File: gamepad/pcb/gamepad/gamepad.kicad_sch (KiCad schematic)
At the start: 9 parts, among them U1 Pico

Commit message: upt(gamepad): working on pcb
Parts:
- renumbered ButtonConnector1 to dPad_east1, ButtonConnector6 to dPad_north1, ButtonConnector2 to dPad_south1, ButtonConnector3 to dPad_west1, JoystickConnector2 to joystick_left1, JoystickConnector1 to joystick_right1, ButtonConnector5 to operators_minus1, ButtonConnector4 to operators_plus1
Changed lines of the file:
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@@
 		(dnp no)
 		(fields_autoplaced yes)
-		(property "Reference" "ButtonConnector4"
+		(property "Reference" "operators_plus1"
 			(at 158.75 111.7599 0)
 			(effects
@@
 			(project "gamepad"
 				(path "/00bcd25f-2f85-4197-8989-5ad786ea0927"
-					(reference "ButtonConnector4")
+					(reference "operators_plus1")
 					(unit 1)
 				)
@@
 		(dnp no)
 		(fields_autoplaced yes)
-		(property "Reference" "ButtonConnector1"
+		(property "Reference" "dPad_east1"
 			(at 158.75 92.7099 0)
 			(effects
@@
 			(project "gamepad"
 				(path "/00bcd25f-2f85-4197-8989-5ad786ea0927"
-					(reference "ButtonConnector1")
+					(reference "dPad_east1")
 					(unit 1)
 				)
@@
 		(dnp no)
 		(fields_autoplaced yes)
-		(property "Reference" "JoystickConnector2"
+		(property "Reference" "joystick_left1"
 			(at 158.75 128.2699 0)
 			(effects
@@
 			(project ""
 				(path "/00bcd25f-2f85-4197-8989-5ad786ea0927"
-					(reference "JoystickConnector2")
+					(reference "joystick_left1")
 					(unit 1)
 				)
@@
 		(dnp no)
 		(fields_autoplaced yes)
-		(property "Reference" "ButtonConnector2"
+		(property "Reference" "dPad_south1"
 			(at 158.75 99.0599 0)
 			(effects
@@
 			(project "gamepad"
 				(path "/00bcd25f-2f85-4197-8989-5ad786ea0927"
-					(reference "ButtonConnector2")
+					(reference "dPad_south1")
 					(unit 1)
 				)
@@
 		(dnp no)
 		(fields_autoplaced yes)
-		(property "Reference" "ButtonConnector6"
+		(property "Reference" "dPad_north1"
 			(at 158.75 86.3599 0)
 			(effects
@@
 			(project ""
 				(path "/00bcd25f-2f85-4197-8989-5ad786ea0927"
-					(reference "ButtonConnector6")
+					(reference "dPad_north1")
 					(unit 1)
 				)
@@
 		(dnp no)
 		(fields_autoplaced yes)
-		(property "Reference" "JoystickConnector1"
+		(property "Reference" "joystick_right1"
 			(at 158.75 142.2399 0)
 			(effects
@@
 			(project "gamepad"
 				(path "/00bcd25f-2f85-4197-8989-5ad786ea0927"
-					(reference "JoystickConnector1")
+					(reference "joystick_right1")
 					(unit 1)
 				)
@@
 		(dnp no)
 		(fields_autoplaced yes)
-		(property "Reference" "ButtonConnector5"
+		(property "Reference" "operators_minus1"
 			(at 158.75 118.1099 0)
 			(effects
@@
 			(project "gamepad"
 				(path "/00bcd25f-2f85-4197-8989-5ad786ea0927"
-					(reference "ButtonConnector5")
+					(reference "operators_minus1")
 					(unit 1)
 				)
@@
 		(dnp no)
 		(fields_autoplaced yes)
-		(property "Reference" "ButtonConnector3"
+		(property "Reference" "dPad_west1"
 			(at 158.75 105.4099 0)
 			(effects
@@
 			(project "gamepad"
 				(path "/00bcd25f-2f85-4197-8989-5ad786ea0927"
-					(reference "ButtonConnector3")
-					(unit 1)
-				)
+					(reference "dPad_west1")
+					(unit 1)
+				)

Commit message: upt: gamepad pcb
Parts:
- added U2: MCU-MCP3008-I_P_DIP16-7.62MM_, MCU-MCP3008:DIP16-2.54-19.2X7.62MM, symbol MCU-MCP3008-I_P_DIP16-7.62MM_:MCU-MCP3008-I_P_DIP16-7.62MM_

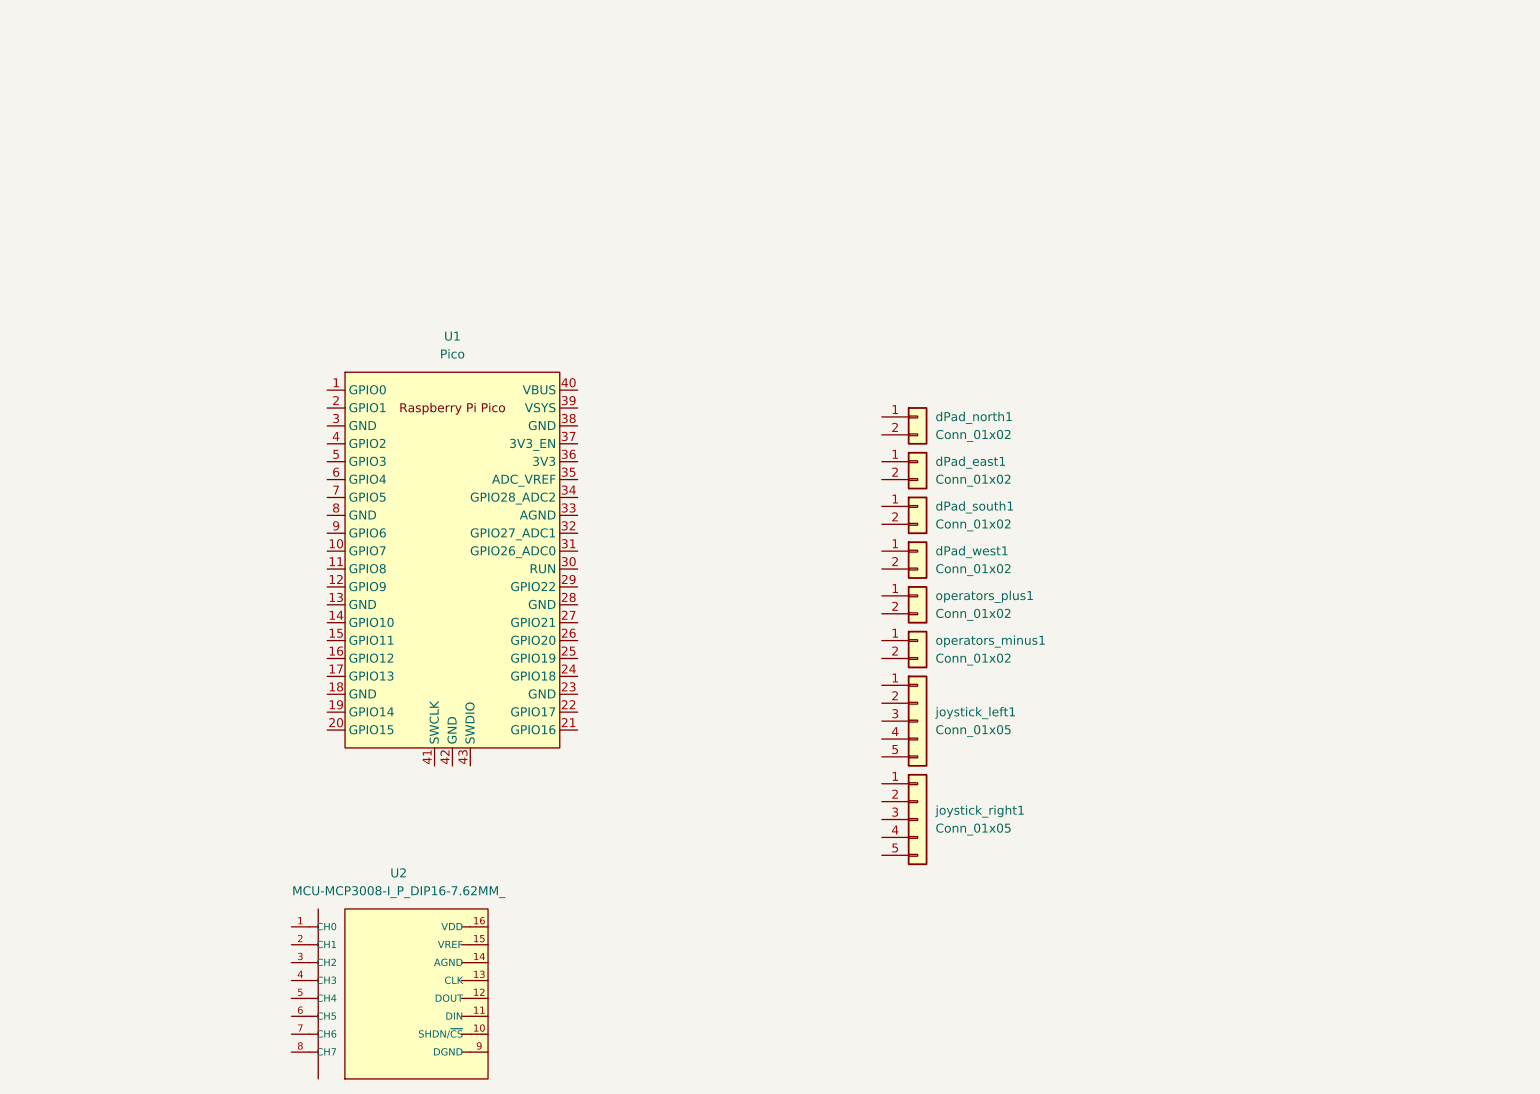
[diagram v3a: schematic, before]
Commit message: upt: start wiring schematic
just gotta make sure it works on a breadboard before ordering a pcb
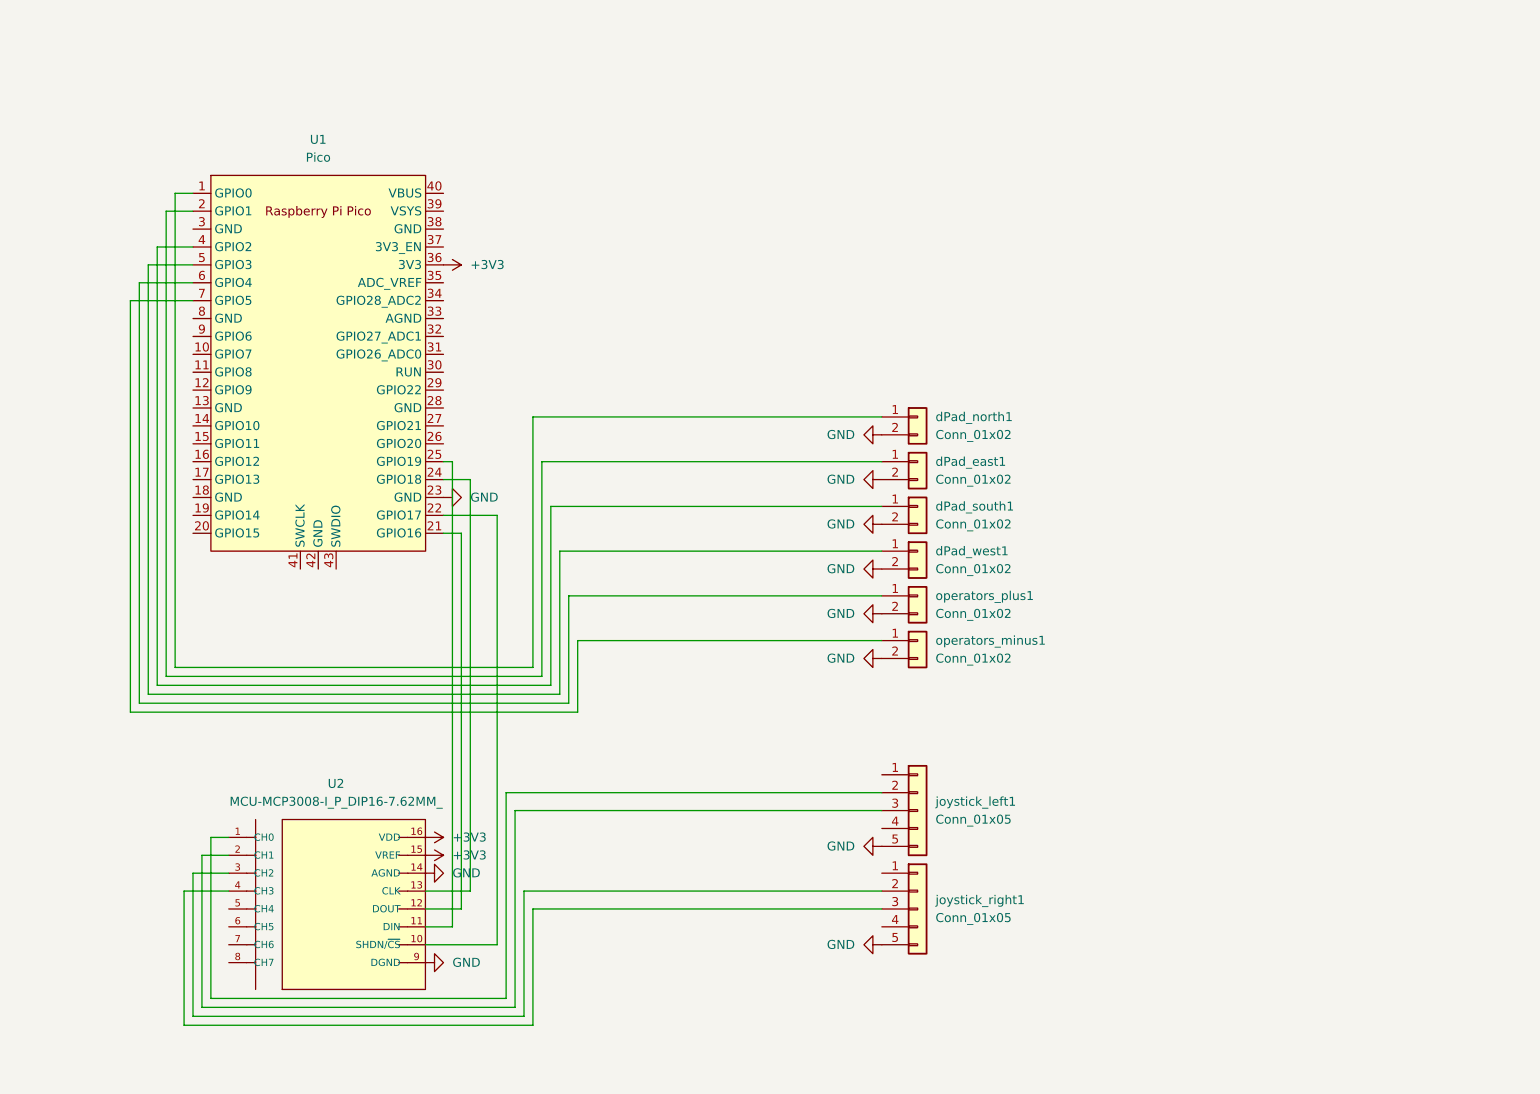
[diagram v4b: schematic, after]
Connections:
- net at operators_plus1.1 (Pin_1): now also U1.6 (GPIO4)
- net GND: now reaches operators_plus1.2 (Pin_2)
- net GND: now also U1.23 (GND), U2.14 (AGND), U2.9 (DGND), dPad_east1.2 (Pin_2), dPad_north1.2 (Pin_2), dPad_south1.2 (Pin_2), dPad_west1.2 (Pin_2), joystick_left1.5 (Pin_5), joystick_right1.5 (Pin_5), operators_minus1.2 (Pin_2)
- net at dPad_east1.1 (Pin_1): now also U1.2 (GPIO1)
- net at joystick_left1.2 (Pin_2): now also U2.1 (CH0)
- net at joystick_left1.3 (Pin_3): now also U2.2 (CH1)
- net at dPad_south1.1 (Pin_1): now also U1.4 (GPIO2)
- net at U2.10 (SHDN/~{CS}): now also U1.22 (GPIO17)
- net at U2.11 (DIN): now also U1.25 (GPIO19)
- net at U2.12 (DOUT): now also U1.21 (GPIO16)
- net at U2.13 (CLK): now also U1.24 (GPIO18)
- net +3V3: now reaches U2.15 (VREF)
- net +3V3: now also U1.36 (3V3), U2.16 (VDD)
- net at U2.3 (CH2): now also joystick_right1.2 (Pin_2)
- net at U2.4 (CH3): now also joystick_right1.3 (Pin_3)
- net at dPad_north1.1 (Pin_1): now also U1.1 (GPIO0)
- net at U1.5 (GPIO3): now also dPad_west1.1 (Pin_1)
- net at U1.7 (GPIO5): now also operators_minus1.1 (Pin_1)
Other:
- company: (none) -> Andrew Arcade
- title: (none) -> Gamepad PCB
- moved on the sheet: U1, U2, joystick_left1, joystick_right1

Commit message: upt: some stuff for the pcb
- routed the traces
- cleaned up the wiring for the schematic
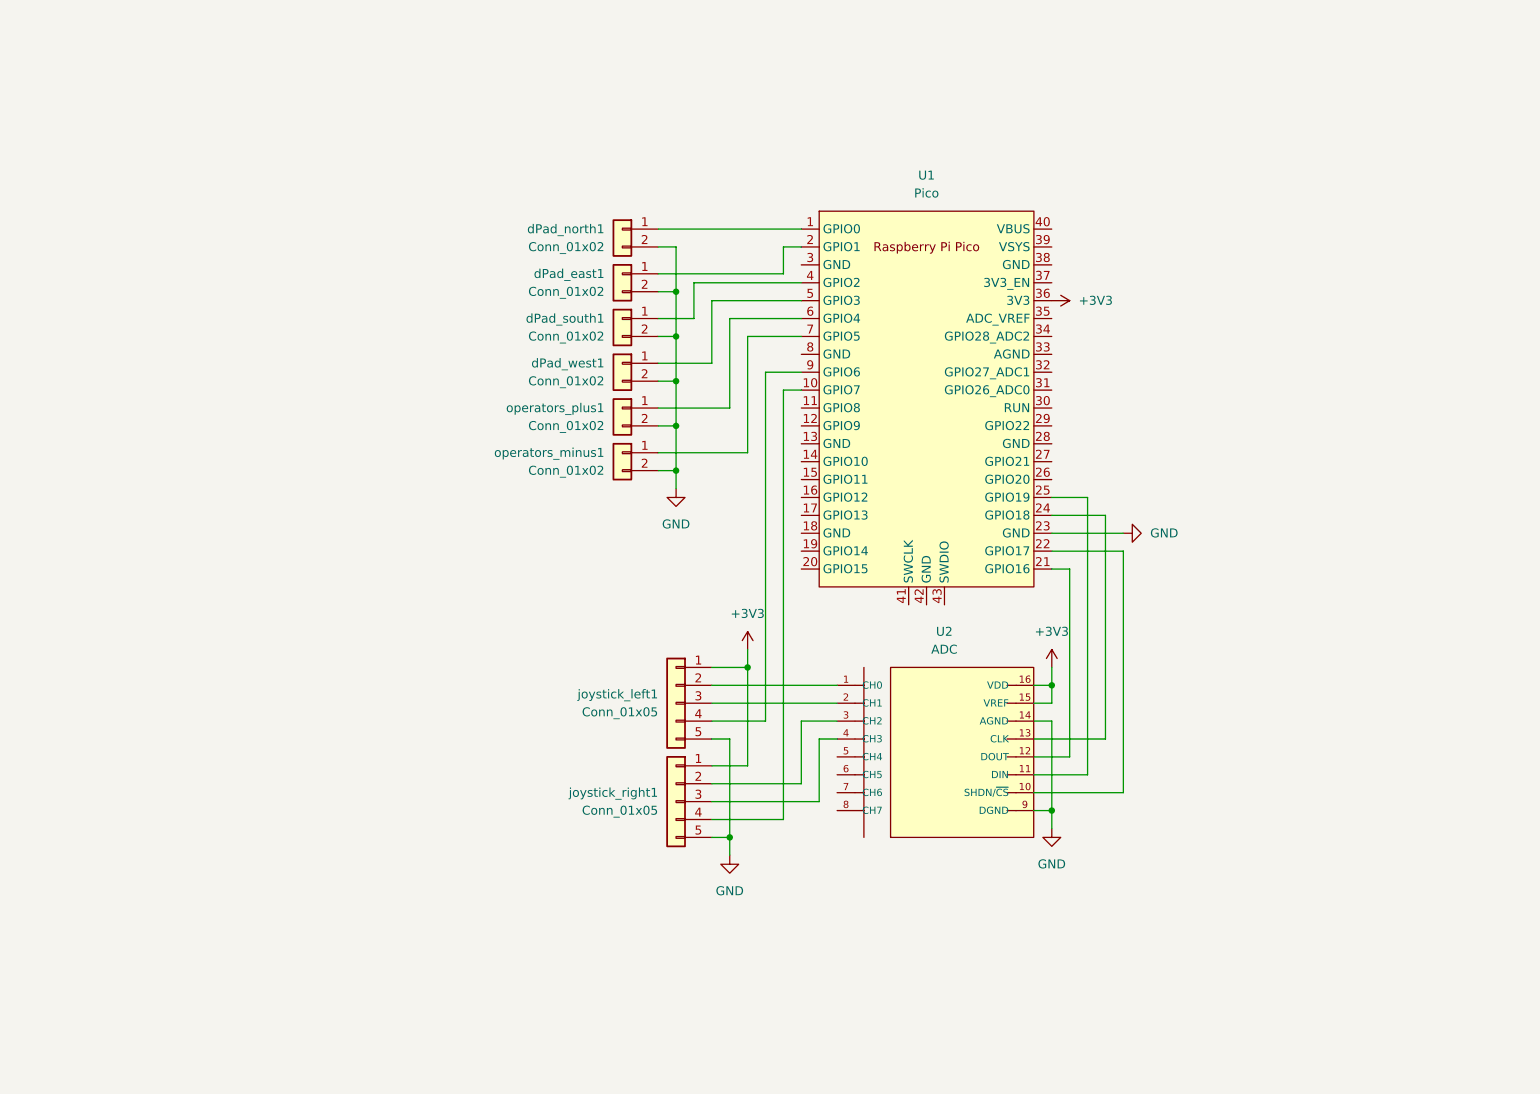
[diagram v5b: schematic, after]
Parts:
- U2: value MCU-MCP3008-I_P_DIP16-7.62MM_ -> ADC
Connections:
- net +3V3: now also joystick_left1.1 (Pin_1), joystick_right1.1 (Pin_1)
- net at joystick_left1.4 (Pin_4): now also U1.9 (GPIO6)
- net at joystick_right1.4 (Pin_4): now also U1.10 (GPIO7)
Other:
- moved on the sheet: U1, U2, dPad_east1, dPad_north1, dPad_south1, dPad_west1, joystick_left1, joystick_right1, operators_minus1, operators_plus1

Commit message: feat: some pcb stuff
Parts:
- added U3: RP2040-ZERO, RP2040-ZERO:MODULE_RP2040-ZERO, symbol RP2040-ZERO:RP2040-ZERO
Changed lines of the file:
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@@
+	)
+	(symbol
+		(lib_id "RP2040-ZERO:RP2040-ZERO")
+		(at 224.79 82.55 0)
+		(unit 1)
+		(exclude_from_sim no)
+		(in_bom yes)
+		(on_board yes)
+		(dnp no)
+		(fields_autoplaced yes)
+		(property "Reference" "U3"
+			(at 224.79 57.15 0)
+			(effects
+				(font
+					(size 1.27 1.27)
+				)
+			)
+		)
+		(property "Value" "RP2040-ZERO"
+			(at 224.79 59.69 0)
+			(effects
+				(font
+					(size 1.27 1.27)
+				)
+			)
+		)
+		(property "Footprint" "RP2040-ZERO:MODULE_RP2040-ZERO"
+			(at 224.79 82.55 0)
+			(effects
+				(font
+					(size 1.27 1.27)
+				)
+				(justify bottom)
+				(hide yes)
+			)
+		)
+		(property "Datasheet" ""
+			(at 224.79 82.55 0)
+			(effects
+				(font
+					(size 1.27 1.27)
+				)
+				(hide yes)
+			)
+		)
+		(property "Description" ""
+			(at 224.79 82.55 0)
+			(effects
+				(font
+					(size 1.27 1.27)
+				)
+				(hide yes)
+			)
+		)
+		(property "MF" "Waveshare Electronics"
+			(at 224.79 82.55 0)
+			(effects
+				(font
+					(size 1.27 1.27)
+				)
+				(justify bottom)
+				(hide yes)
+			)
+		)
+		(property "MAXIMUM_PACKAGE_HEIGHT" "5.35mm"
+			(at 224.79 82.55 0)
+			(effects
+				(font
+					(size 1.27 1.27)
+				)
+				(justify bottom)
+				(hide yes)
+			)
+		)
+		(property "Package" "Package"
+			(at 224.79 82.55 0)
+			(effects
+				(font
+					(size 1.27 1.27)
+				)
+				(justify bottom)
+				(hide yes)
+			)
+		)
+		(property "Price" "None"
+			(at 224.79 82.55 0)
+			(effects
+				(font
+					(size 1.27 1.27)
+				)
+				(justify bottom)
+				(hide yes)
+			)
+		)
+		(property "Check_prices" "https://www.snapeda.com/parts/RP2040-ZERO/Waveshare+Electronics/view-part/?ref=eda"
+			(at 224.79 82.55 0)
+			(effects
+				(font
+					(size 1.27 1.27)
+				)
+				(justify bottom)
+				(hide yes)
+			)
+		)
+		(property "STANDARD" "Manufacturer Recommendations"
+			(at 224.79 82.55 0)
+			(effects
+				(font
+					(size 1.27 1.27)
+				)
+				(justify bottom)
+				(hide yes)
+			)
+		)
+		(property "PARTREV" "NA"
+			(at 224.79 82.55 0)
+			(effects
+				(font
+					(size 1.27 1.27)
+				)
+				(justify bottom)
+				(hide yes)
+			)
+		)
+		(property "SnapEDA_Link" "https://www.snapeda.com/parts/RP2040-ZERO/Waveshare+Electronics/view-part/?ref=snap"
+			(at 224.79 82.55 0)
+			(effects
+				(font
+					(size 1.27 1.27)
+				)
+				(justify bottom)
+				(hide yes)
+			)
+		)
+		(property "MP" "RP2040-ZERO"
+			(at 224.79 82.55 0)
+			(effects
+				(font
+					(size 1.27 1.27)
+				)
+				(justify bottom)
+				(hide yes)
+			)
+		)
+		(property "Description_1" "Low-Cost, High-Performance Pico-Like MCU Board Based On Raspberry Pi Microcontroller RP2040"
+			(at 224.79 82.55 0)
+			(effects
+				(font
+					(size 1.27 1.27)
+				)
+				(justify bottom)
+				(hide yes)
+			)
+		)
+		(property "Availability" "Not in stock"
+			(at 224.79 82.55 0)
+			(effects
+				(font
+					(size 1.27 1.27)
+				)
+				(justify bottom)
+				(hide yes)
+			)
+		)
+		(property "MANUFACTURER" "Waveshare"
+			(at 224.79 82.55 0)
+			(effects
+				(font
+					(size 1.27 1.27)
+				)
+				(justify bottom)
+				(hide yes)
+			)
+		)
+		(pin "10"
+		)
+		(pin "12"
+		)
+		(pin "1"
+		)
+		(pin "5"
+		)
+		(pin "17"
+		)
+		(pin "19"
+		)
+		(pin "8"
+		)
+		(pin "6"
+		)
+		(pin "9"
+		)
+		(pin "23"
+		)
+		(pin "21"
+		)
+		(pin "18"
+		)
+		(pin "22"
+		)
+		(pin "11"
+		)
+		(pin "14"
+		)
+		(pin "20"
+		)
+		(pin "15"
+		)
+		(pin "13"
+		)
+		(pin "16"
+		)
+		(pin "2"
+		)
+		(pin "3"
+		)
+		(pin "4"
+		)
+		(pin "7"
+		)
+		(instances
+			(project ""
+				(path "/00bcd25f-2f85-4197-8989-5ad786ea0927"
+					(reference "U3")
+					(unit 1)
+				)
+			)
+		)
 	)
 	(symbol
